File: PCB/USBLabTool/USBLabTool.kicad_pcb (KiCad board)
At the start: 4 copper layers, 79.4 x 56.2 mm, 228 parts, among them J1 Conn_01x06_Pin, J10 T_pwm, J11 T_buf, J12 T_buf, J13 ADC2, J14 ADC1, J15 +3.3VA, J16 +3.3VA, J17 2x01, J19 T_N5V, J2 Conn_02x12_Odd_Even, J20 USB_C_Receptacle, J3 T_att, J4 T_att, J5 T_acdc, J6 T_acdc, J7 T_amp, J8 T_amp, J9 T_pwm, K1 G5V-2, K2 G5V-2, SW1 SW_Push, U1 AQY284SX, U10 Opamp_Quad, U11 DG403, U12 STM32H562VGTx, U13 r1283, U14 ST1L05APU33R, U15 ST1L05APU33R, U16 LTC1983ES6-5#TRPBF, U17 TCPP01-M12, U18 74HC245, U2 AQY284SX, U20 74HC245, U3 CD74HC4316PWR, U4 LMP7718, U5 CD74HC4316PWR, U6 LMP7718, U7 OPA863, U8 OPA863, U9 Opamp_Quad, Y1 32.768kHz

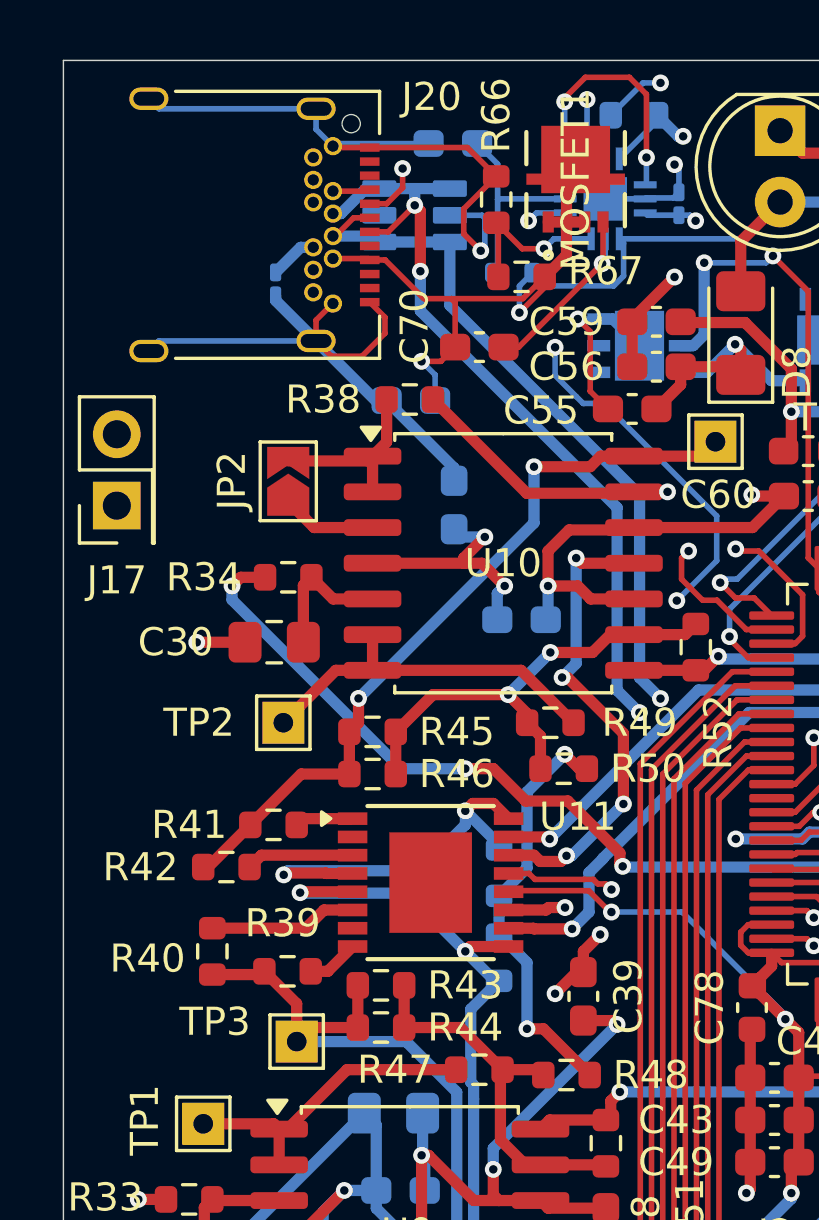
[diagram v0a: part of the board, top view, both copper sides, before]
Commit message: change mosfet footprint
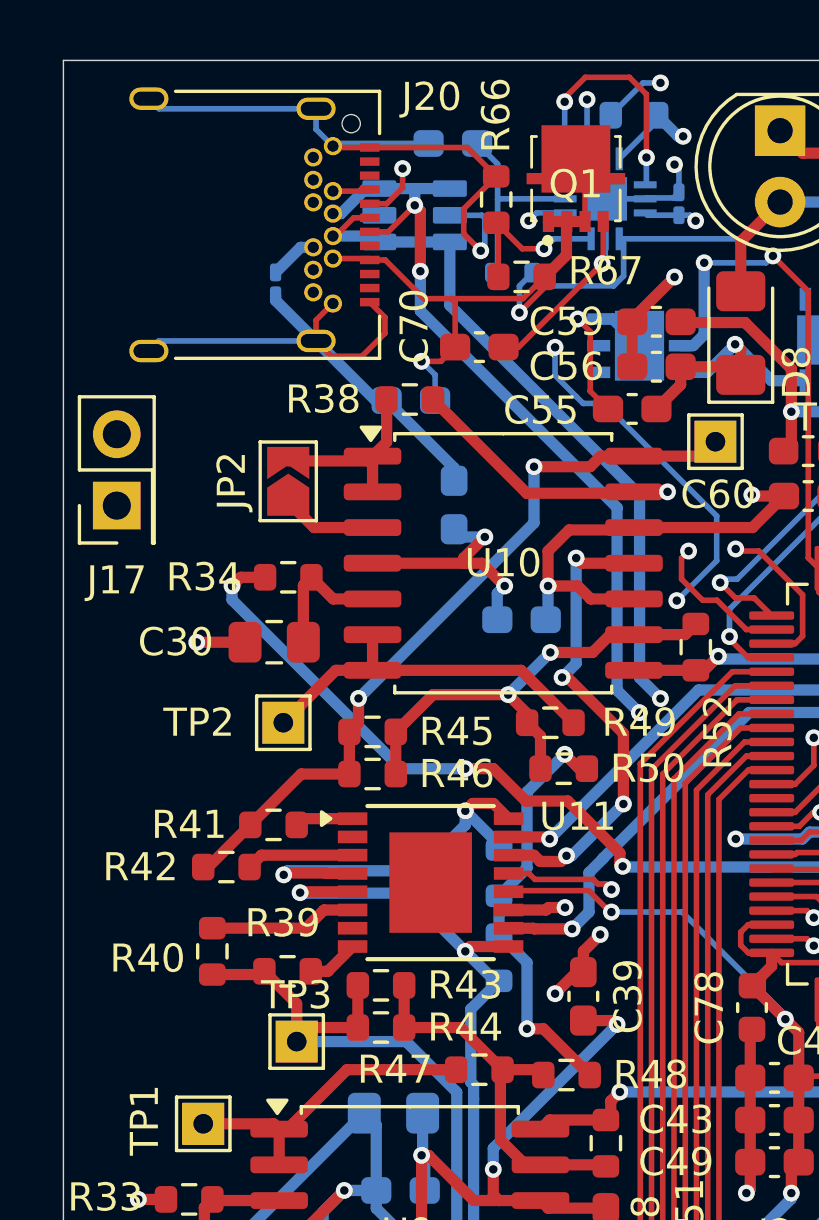
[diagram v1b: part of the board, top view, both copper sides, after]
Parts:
- removed MOSFET1: STL11N3LLH6, userfp:POWERFLAT-3p3X3p3_STM
- added Q1: STL11N3LLH6, userfp:STL20N6F7_snapmagic, F.Cu at (128.2, 69.8)
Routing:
- net +5V: track 246.1 -> 243.5 mm

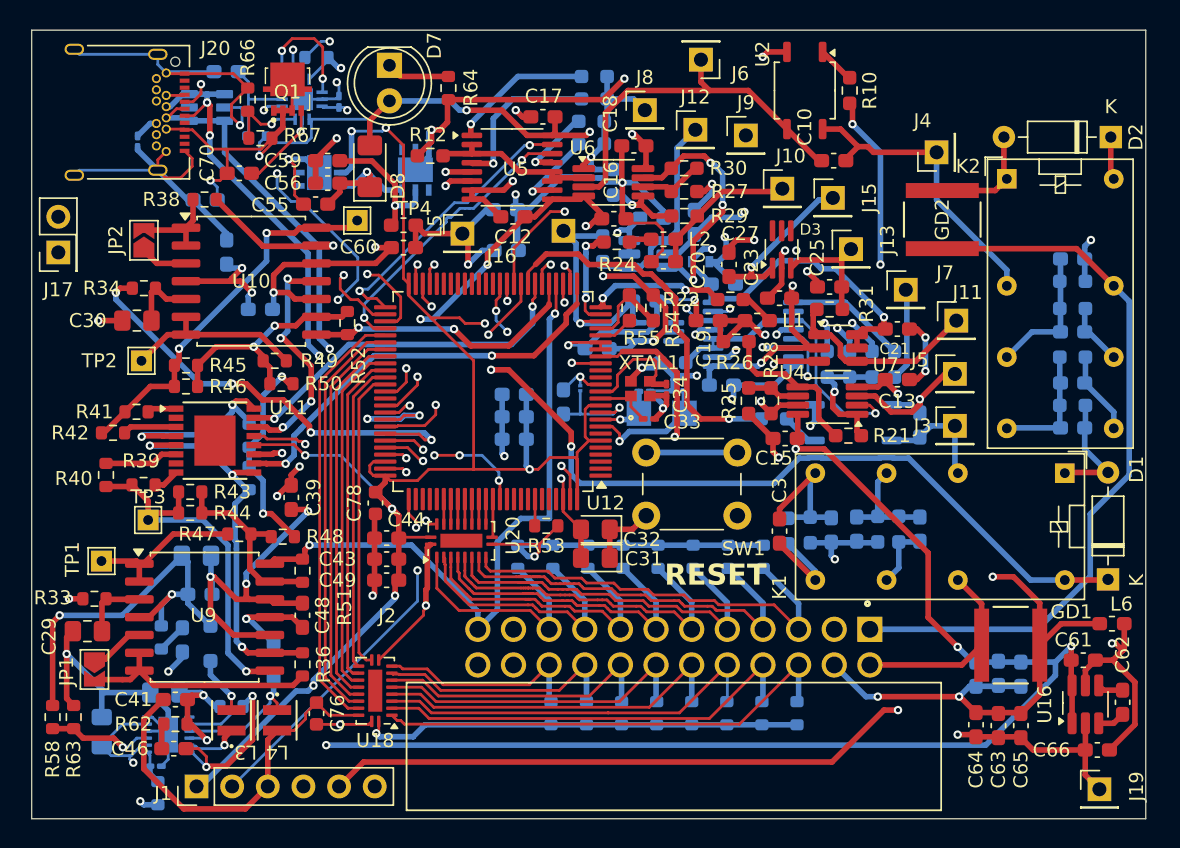
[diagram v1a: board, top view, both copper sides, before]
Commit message: fix board wiring as mentioned in email by Prof. Kaps
This is the follow up, wiring, of the previous schematic fix.
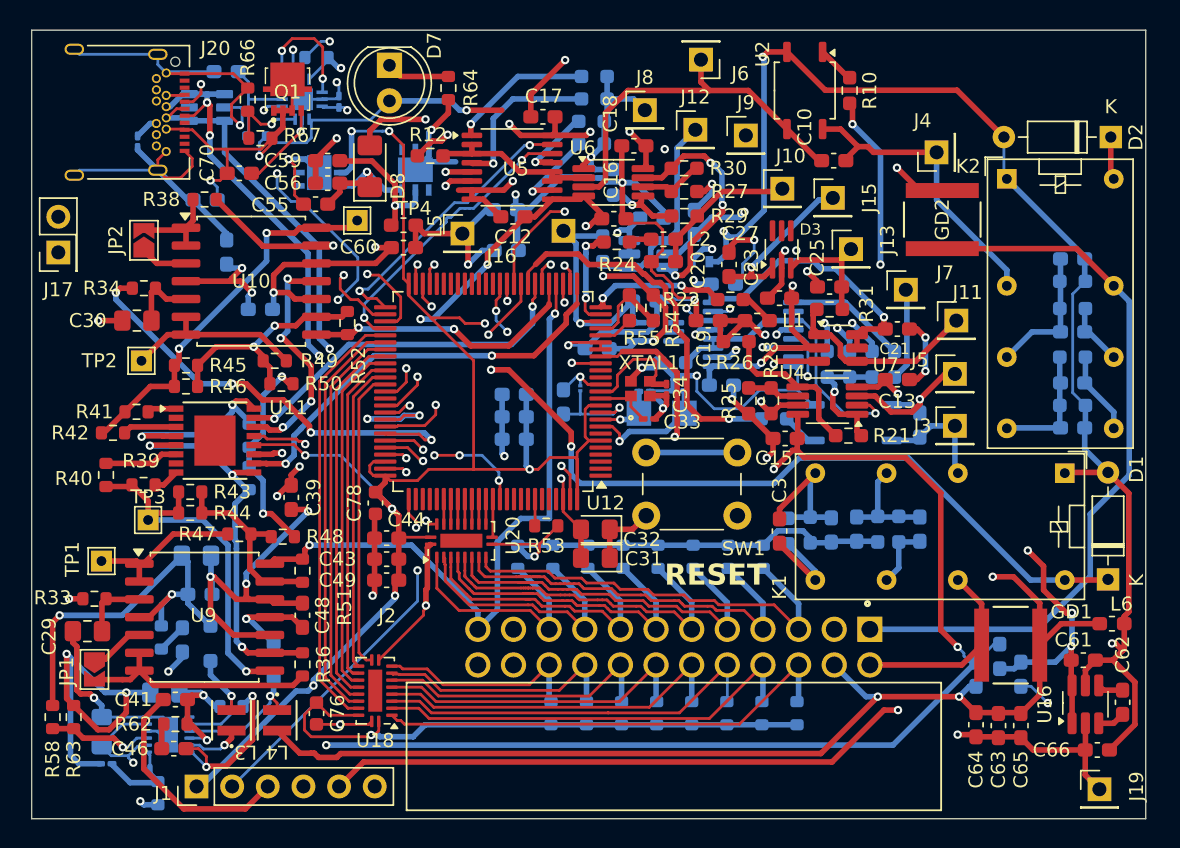
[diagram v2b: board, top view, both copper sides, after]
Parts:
- removed C69: 100n, Capacitor_SMD:C_0603_1608Metric_Pad1.08x0.95mm_HandSolder
- added L7: 4.7uH, Inductor_SMD:L_0603_1608Metric_Pad1.05x0.95mm_HandSolder, B.Cu at (179.0, 110.2)
- L1, L2: value 10u -> 10uH
- L3, L4: value 4.7u -> 4.7uH
- L5, L6: value 47u -> 47uH
- moved C42 3.52 mm to (115.3, 117.8), turned to 180 degrees
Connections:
- C1 pad 1: GNDA -> GND
- C11 pad 2: GND -> GNDA
- C12 pad 2: GND -> GNDA
- C14 pad 1: +5V -> +5VCLEAN
- C14 pad 2: GND -> GNDA
- C15 pad 1: +5V -> +5VCLEAN
- C17 pad 1: +5V -> +5VCLEAN
- C17 pad 2: GND -> GNDA
- C18 pad 1: +5V -> +5VCLEAN
- C21 pad 2: +5V -> +5VCLEAN
- C22 pad 2: +5V -> +5VCLEAN
- C29 pad 2: GNDA -> GND
- C37 pad 1: +5V -> +5VCLEAN
- C37 pad 2: GNDA -> GND
- C4 pad 2: GNDA -> GND
- C5 pad 1: GNDA -> GND
- C56 pad 2: GNDA -> GND
- C59 pad 1: GNDA -> GND
- C67 pad 2: GNDA -> GND
- C68 pad 1: +5V -> +5VCLEAN
- C8 pad 2: GNDA -> GND
- D1 pad 2: GNDA -> GND
- D2 pad 2: GNDA -> GND
- D8 pad 2: +5V -> +5VCLEAN
- K1 pad 1: GNDA -> GND
- K2 pad 1: GNDA -> GND
- L3 pad 1: +5V -> +5VCLEAN
- L4 pad 2: GND -> GNDA
- R2 pad 1: GNDA -> GND
- R3 pad 1: GNDA -> GND
- R5 pad 1: GNDA -> GND
- R64 pad 2: GNDA -> GND
- R8 pad 1: GNDA -> GND
- U1 pad 2: GNDA -> GND
- U13 pad 10: GNDA -> GND
- U13 pad 11: +5V -> +5VCLEAN
- U13 pad 12: GNDA -> GND
- U13 pad 13: GNDA -> GND
- U13 pad 5: +5V -> +5VCLEAN
- U13 pad 8: +5V -> +5VCLEAN
- U15 pad 6: GNDA -> GND
- U15 pad 7: GNDA -> GND
- U2 pad 2: GNDA -> GND
- U3 pad 16: +5V -> +5VCLEAN
- U4 pad 8: +5V -> +5VCLEAN
- U5 pad 16: +5V -> +5VCLEAN
- U6 pad 8: +5V -> +5VCLEAN
- U7 pad 5: +5V -> +5VCLEAN
- U7 pad 6: +5V -> +5VCLEAN
- U8 pad 5: +5V -> +5VCLEAN
- U8 pad 6: +5V -> +5VCLEAN
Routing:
- net +5VCLEAN: track 0.00 -> 188.9 mm, vias 0 -> 12
- net GND: track 243.3 -> 380.8 mm, vias 24 -> 27
- net +5V: track 243.5 -> 167.9 mm, vias 14 -> 8
- net GNDA: track 320.2 -> 331.2 mm, vias 27 -> 25
- net Net-(U13-Vref): track 2.42 -> 6.31 mm
- net Net-(U6-OUT_B): track 17.5 -> 16.6 mm

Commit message: Update USBLabTool.kicad_pcb
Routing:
- net +5V: track 167.9 -> 198.1 mm, vias 8 -> 9
- net GND: track 380.8 -> 375.7 mm
- net GNDA: track 331.2 -> 333.2 mm
- net UCPD_CC2: track 53.2 -> 54.0 mm
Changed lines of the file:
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@@
 		(tags "test point THT pad rectangle square")
 		(property "Reference" "TP3"
-			(at 0 -1.648 0)
+			(at -2.606 0.046 0)
 			(layer "F.SilkS")
 			(effects
@@
 		(descr "<b>PowerFLAT 3.3x3.3</b><br>")
 		(property "Reference" "Q1"
-			(at 0 0.2 0)
+			(at -0.015 -0.775 0)
 			(layer "F.SilkS")
 			(effects
@@
 	)
 	(segment
+		(start 143.4435 78.844)
+		(end 143.4435 78.3065)
+		(width 0.4)
+		(layer "F.Cu")
+		(net 2)
+	)
+	(segment
 		(start 173.2989 76.9739)
 		(end 171.675 75.35)
@@
 	)
 	(segment
+		(start 143.4435 78.3065)
+		(end 144.5 77.25)
+		(width 0.4)
+		(layer "F.Cu")
+		(net 2)
+	)
+	(segment
 		(start 127.5 115.4605)
 		(end 129.1145 117.075)
@@
 	)
 	(segment
-		(start 141.381 76.944)
-		(end 140.431 76.944)
-		(width 0.4)
-		(layer "F.Cu")
-		(net 14)
-	)
-	(segment
 		(start 147.984021 82.322021)
 		(end 148.381 82.719)
@@
 	)
 	(segment
-		(start 142.1935 77.594)
-		(end 143.4435 78.844)
-		(width 0.4)
-		(layer "F.Cu")
-		(net 14)
-	)
-	(segment
 		(start 129.45 114.325)
 		(end 130.306 113.469)
@@
 	)
 	(segment
-		(start 137.922799 74.925)
-		(end 140.225 74.925)
-		(width 0.4)
-		(layer "B.Cu")
-		(net 14)
-	)
-	(segment
 		(start 157.411509 90.168753)
 		(end 156 90.168753)
@@
 	)
 	(segment
-		(start 143.520636 71.25)
-		(end 141 71.25)
-		(width 0.4)
-		(layer "F.Cu")
-		(net 16)
-	)
-	(segment
 		(start 119.596 72.594)
 		(end 120.856 72.594)
@@
 	)
 	(via
+		(at 171.425 80.925)
+		(size 0.6)
+		(drill 0.3)
+		(layers "F.Cu" "B.Cu")
+		(net 16)
+	)
+	(via
 		(at 184.106 109.444)
 		(size 0.6)
@@
 	)
 	(via
-		(at 141 71.25)
+		(at 171.425 76.45)
 		(size 0.6)
 		(drill 0.3)
@@
 	)
 	(segment
+		(start 171.425 80.925)
+		(end 171.425 76.45)
+		(width 0.4)
+		(layer "B.Cu")
+		(net 16)
+	)
+	(segment
 		(start 129.937437 72.045235)
 		(end 129.937437 73.213977)
@@
 	)
 	(segment
-		(start 141 71.25)
-		(end 140.5 71.25)
-		(width 0.4)
-		(layer "B.Cu")
-		(net 16)
-	)
-	(segment
 		(start 184.15 107.075)
 		(end 184.15 109.4)
@@
 	)
 	(segment
-		(start 157.056 81.944)
-		(end 157.056 82.044)
+		(start 171.425 76.45)
+		(end 171.425 76.425)
 		(width 0.4)
 		(layer "B.Cu")
@@
 	)
 	(segment
-		(start 139.834 70.584)
-		(end 135.506 70.584)
+		(start 157.056 81.944)
+		(end 157.056 82.044)
 		(width 0.4)
 		(layer "B.Cu")
@@
 	)
 	(segment
-		(start 140.5 71.25)
-		(end 139.834 70.584)
-		(width 0.4)
-		(layer "B.Cu")
-		(net 16)
-	)
-	(segment
 		(start 158.5 81.143998)
 		(end 157.856002 81.143998)
@@
 	)
 	(segment
+		(start 149.475 73.8)
+		(end 146.925 71.25)
+		(width 0.4)
+		(layer "In1.Cu")
+		(net 16)
+	)
+	(segment
+		(start 146.925 71.25)
+		(end 139 71.25)
+		(width 0.4)
+		(layer "In1.Cu")
+		(net 16)
+	)
+	(segment
 		(start 177.725 99.35)
 		(end 180.7 102.325)
@@
 	)
 	(segment
+		(start 135.615 70.475)
+		(end 135.506 70.584)
+		(width 0.4)
+		(layer "In1.Cu")
+		(net 16)
+	)
+	(segment
+		(start 154.9 73.8)
+		(end 149.475 73.8)
+		(width 0.4)
+		(layer "In1.Cu")
+		(net 16)
+	)
+	(segment
 		(start 158.5 81.143998)
 		(end 159.581002 81.143998)
@@
 	)
 	(segment
-		(start 154.9 73.8)
-		(end 155.125 74.025)
+		(start 155.125 74.025)
+		(end 154.9 73.8)
 		(width 0.4)
 		(layer "In1.Cu")
@@
 	)
 	(segment
+		(start 139 71.25)
+		(end 138.225 70.475)
+		(width 0.4)
+		(layer "In1.Cu")
+		(net 16)
+	)
+	(segment
 		(start 165.175 79.225)
 		(end 166.25 80.3)
@@
 	)
 	(segment
+		(start 138.225 70.475)
+		(end 135.615 70.475)
+		(width 0.4)
+		(layer "In1.Cu")
+		(net 16)
+	)
+	(segment
 		(start 180.7 102.325)
 		(end 181.45 103.075)
@@
 	)
 	(segment
-		(start 141 71.25)
-		(end 146.925 71.25)
-		(width 0.4)
-		(layer "In1.Cu")
-		(net 16)
-	)
-	(segment
 		(start 165.1 79.3)
 		(end 165.175 79.225)
@@
 	)
 	(segment
-		(start 149.475 73.8)
-		(end 154.9 73.8)
-		(width 0.4)
-		(layer "In1.Cu")
-		(net 16)
-	)
-	(segment
 		(start 169.325 82.525)
 		(end 170.55 83.75)
@@
 	)
 	(segment
-		(start 146.925 71.25)
-		(end 149.475 73.8)
-		(width 0.4)
-		(layer "In1.Cu")
-		(net 16)
-	)
-	(segment
 		(start 181.45 105.975)
 		(end 182.55 107.075)
@@
 	)
 	(segment
-		(start 177.55 99.175)
-		(end 177.55 83.425)
+		(start 156 70.975)
+		(end 155.125 71.85)
+		(width 0.4)
+		(layer "In2.Cu")
+		(net 16)
+	)
+	(segment
+		(start 165.95 70.975)
+		(end 156 70.975)
 		(width 0.4)
 		(layer "In2.Cu")
@@
 	)
 	(segment
-		(start 156.9 75.8)
-		(end 158.85 75.8)
+		(start 171.425 80.925)
+		(end 174.825 80.925)
 		(width 0.4)
 		(layer "In2.Cu")
@@
 	)
 	(segment
-		(start 181 102.625)
-		(end 177.55 99.175)
+		(start 177.55 99.175)
+		(end 181 102.625)
+		(width 0.4)
+		(layer "In2.Cu")
+		(net 16)
+	)
+	(segment
+		(start 156.9 75.8)
+		(end 158.85 75.8)
 		(width 0.4)
 		(layer "In2.Cu")
@@
 	)
 	(segment
+		(start 177.55 83.65)
+		(end 177.55 99.175)
+		(width 0.4)
+		(layer "In2.Cu")
+		(net 16)
+	)
+	(segment
+		(start 174.825 80.925)
+		(end 177.55 83.65)
+		(width 0.4)
+		(layer "In2.Cu")
+		(net 16)
+	)
+	(segment
 		(start 159.45 76.4)
 		(end 159.45 76.6)
@@
 	)
 	(segment
+		(start 155.125 71.85)
+		(end 155.125 74.025)
+		(width 0.4)
+		(layer "In2.Cu")
+		(net 16)
+	)
+	(segment
+		(start 171.425 76.45)
+		(end 165.95 70.975)
+		(width 0.4)
+		(layer "In2.Cu")
+		(net 16)
+	)
+	(segment
 		(start 160.8435 86.244)
 		(end 159.906 86.244)
@@
 	)
 	(segment
-		(start 134.5 78.301)
-		(end 127.841466 71.642466)
-		(width 0.2)
-		(layer "In2.Cu")
-		(net 42)
-	)
-	(segment
 		(start 117.5 67)
 		(end 118.25 66.25)
@@
 	)
 	(segment
+		(start 133.92647 82.92647)
+		(end 133.5 82.5)
+		(width 0.2)
+		(layer "In2.Cu")
+		(net 42)
+	)
+	(segment
+		(start 133.5 81.150058)
+		(end 134.5 80.150058)
+		(width 0.2)
+		(layer "In2.Cu")
+		(net 42)
+	)
+	(segment
 		(start 133.5 82.5)
 		(end 133.5 81.150058)
@@
 	(segment
 		(start 134.5 80.150058)
-		(end 134.5 78.301)
+		(end 134.5 77.925)
 		(width 0.2)
 		(layer "In2.Cu")
@@
 	)
 	(segment
-		(start 117.5 70.798)
-		(end 117.5 67)
-		(width 0.4)
+		(start 134.5 77.925)
+		(end 133.75 77.175)
+		(width 0.2)
 		(layer "In2.Cu")
 		(net 42)
 	)
 	(segment
-		(start 133.5 81.150058)
-		(end 134.5 80.150058)
+		(start 129.774 73.575)
+		(end 128.9 73.575)
 		(width 0.2)
 		(layer "In2.Cu")
@@
 	)
 	(segment
-		(start 127.841466 71.642466)
-		(end 127.841466 67.016318)
+		(start 133.374 77.175)
+		(end 129.774 73.575)
 		(width 0.2)
 		(layer "In2.Cu")
@@
 	)
 	(segment
+		(start 133.75 77.175)
+		(end 133.374 77.175)
+		(width 0.2)
+		(layer "In2.Cu")
+		(net 42)
+	)
+	(segment
+		(start 117.5 70.798)
+		(end 117.5 67)
+		(width 0.4)
+		(layer "In2.Cu")
+		(net 42)
+	)
+	(segment
 		(start 126.266318 67.016318)
 		(end 127.841466 67.016318)
@@
 	)
 	(segment
-		(start 133.92647 82.92647)
-		(end 133.5 82.5)
+		(start 128.9 73.575)
+		(end 127.841466 72.516466)
 		(width 0.2)
 		(layer "In2.Cu")
@@
 	)
 	(segment
+		(start 127.841466 72.516466)
+		(end 127.841466 67.016318)
+		(width 0.2)
+		(layer "In2.Cu")
+		(net 42)
+	)
+	(segment
 		(start 133.66 117.7)
 		(end 131.916 119.444)
@@
 	(segment
 		(start 149.876 74.5865)
-		(end 149.2635 75.199)
+		(end 149.49375 74.96875)
 		(width 0.4)
 		(layer "F.Cu")
@@
 	)
 	(segment
-		(start 149.2635 75.199)
-		(end 149.2635 75.324)
+		(start 149.49375 75.26875)
+		(end 149.351 75.4115)
 		(width 0.4)
 		(layer "F.Cu")
@@
 	)
 	(segment
-		(start 149.2635 75.324)
-		(end 149.351 75.4115)
+		(start 149.49375 74.96875)
+		(end 149.49375 75.26875)
 		(width 0.4)
 		(layer "F.Cu")

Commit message: final version prototype
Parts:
- D1: footprint Diode_THT:D_DO-35_SOD27_P7.62mm_Horizontal -> Diode_SMD:D_SOD-323_HandSoldering
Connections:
- C1 pad 1: GND -> GNDA
- C37 pad 1: +5VCLEAN -> +5V
- C4 pad 2: GND -> GNDA
- C42 pad 2: GNDA -> GND
- C5 pad 1: GND -> GNDA
- C8 pad 2: GND -> GNDA
- D8 pad 2: +5VCLEAN -> +5V
- L3 pad 1: +5VCLEAN -> +5V
- L4 pad 2: GNDA -> GND
- R2 pad 1: GND -> GNDA
- R3 pad 1: GND -> GNDA
- R5 pad 1: GND -> GNDA
- R8 pad 1: GND -> GNDA
- U13 pad 11: +5VCLEAN -> +5V
- U13 pad 5: +5VCLEAN -> +5V
- U13 pad 8: +5VCLEAN -> +5V
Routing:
- net +5VCLEAN: track 188.9 -> 97.8 mm, vias 12 -> 7
- net +5V: track 198.1 -> 265.4 mm, vias 9 -> 11
- net GND: track 375.7 -> 350.9 mm, vias 27 -> 28
- net GNDA: track 333.2 -> 334.5 mm, vias 25 -> 27

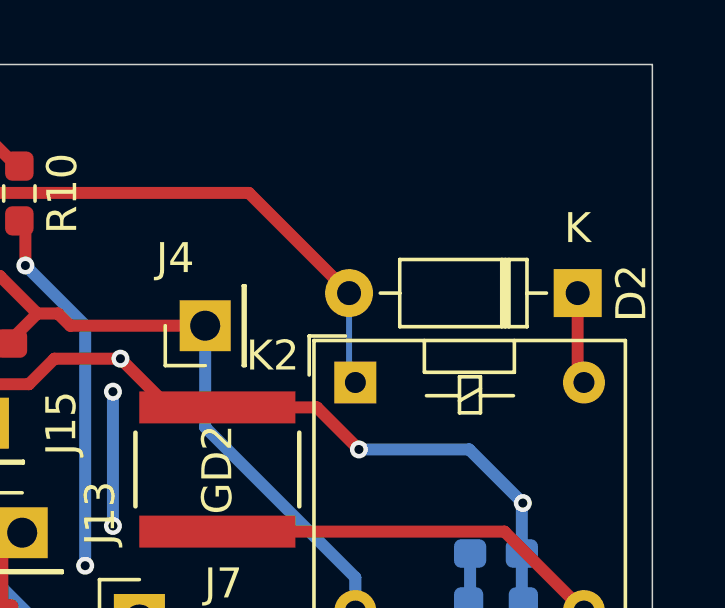
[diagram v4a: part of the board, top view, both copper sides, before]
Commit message: change scope diode footprint
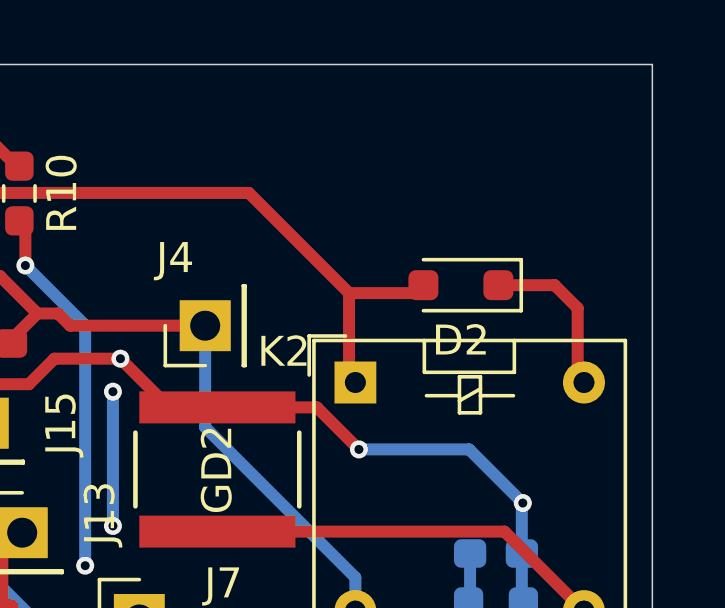
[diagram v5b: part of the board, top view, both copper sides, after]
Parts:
- D2: footprint Diode_THT:D_DO-35_SOD27_P7.62mm_Horizontal -> Diode_SMD:D_SOD-323_HandSoldering
- moved D2 3.90 mm to (183.0, 72.9)
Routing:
- net CH0_attenuate: track 49.4 -> 51.9 mm
- net GND: track 350.9 -> 353.2 mm
